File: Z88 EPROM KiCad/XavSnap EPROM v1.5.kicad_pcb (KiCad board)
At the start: 2 copper layers, 50.5 x 53.3 mm, 5 parts, among them J1 Conn_Z88, U1 NEC_ROM

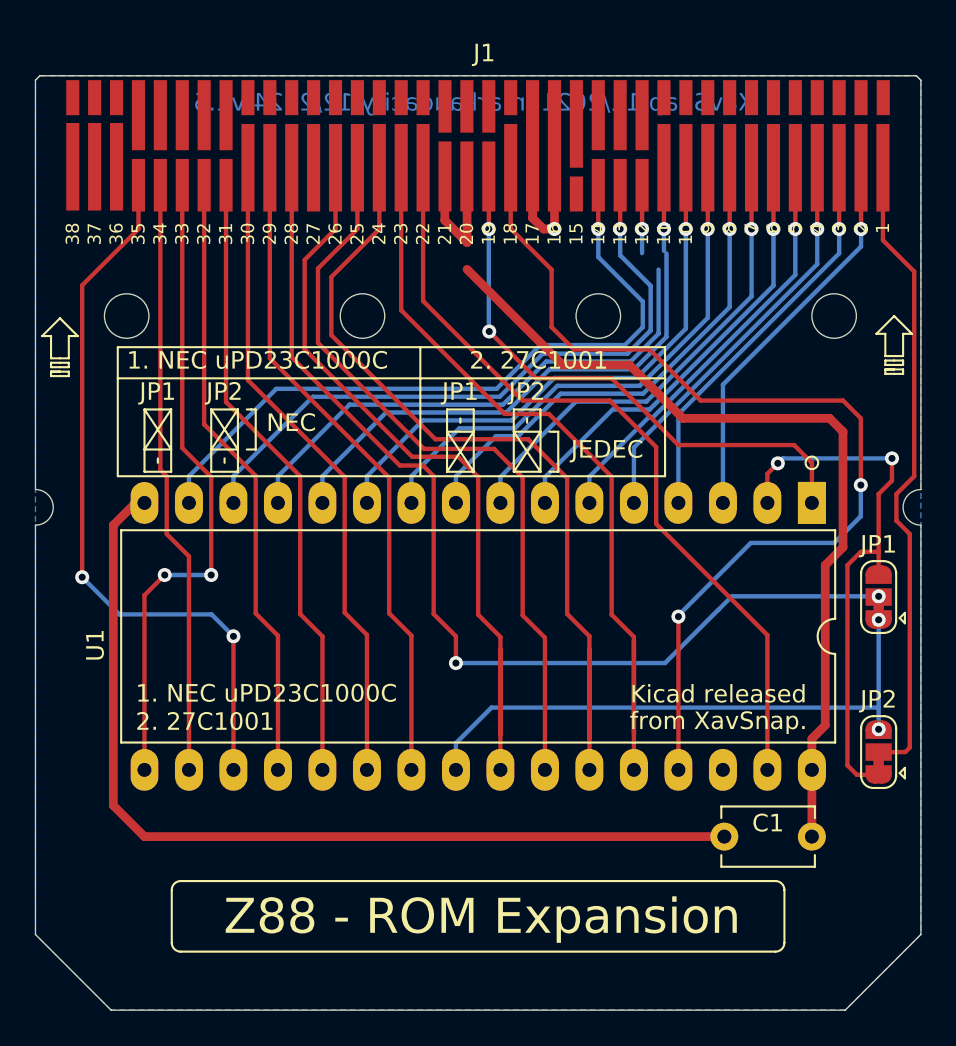
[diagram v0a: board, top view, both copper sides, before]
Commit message: fixed trace connections to edge connector
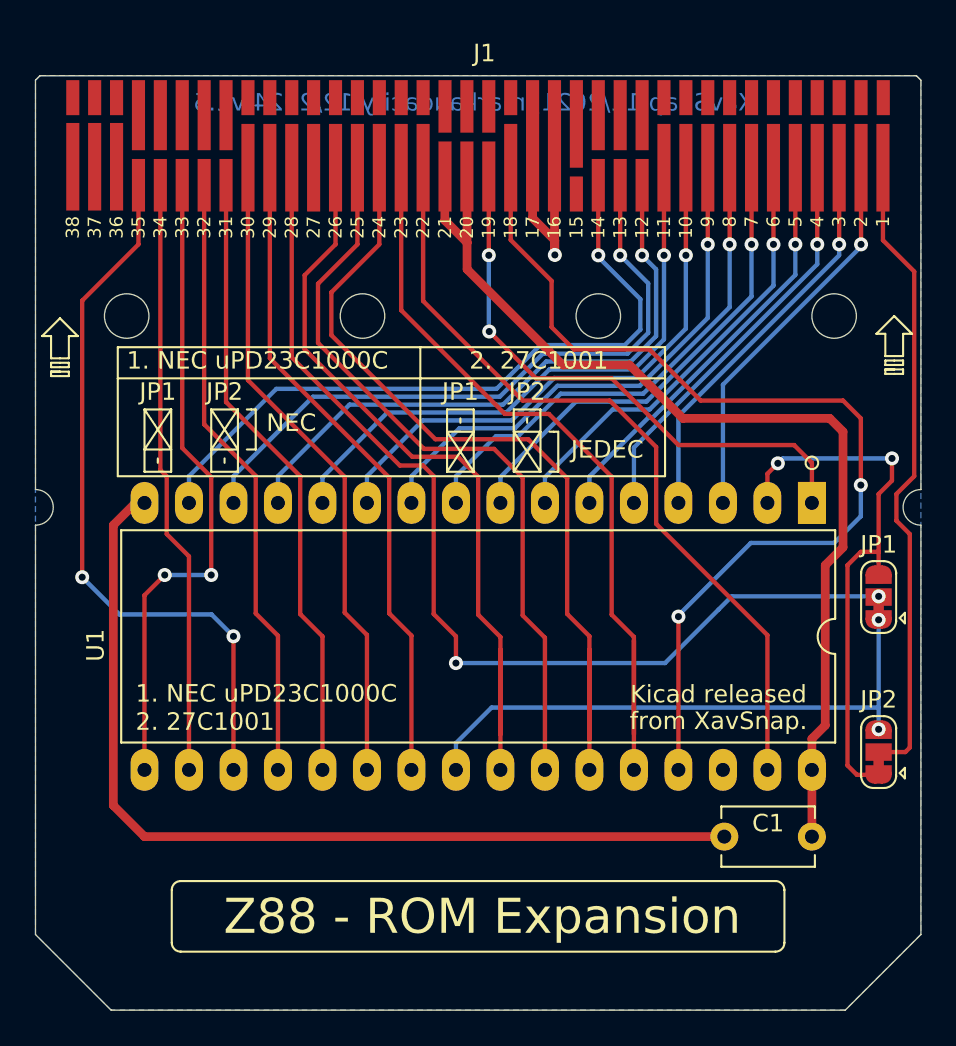
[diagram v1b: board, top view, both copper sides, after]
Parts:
- moved J1 23.2 mm to (141.0, 63.0)
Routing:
- net GND: track 64.6 -> 67.2 mm
- net VCC: track 56.0 -> 57.6 mm
- net /D0: track 34.3 -> 35.5 mm
